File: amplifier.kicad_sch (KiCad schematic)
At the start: 14 parts, among them U1 OPA2188, U3 ADS1254E

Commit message: added simulation
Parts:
- added FB4: FerriteBead, Inductor_SMD:L_0402_1005Metric, symbol Device:FerriteBead
- added R61: 1500, symbol Device:R
- added V1: 3, symbol Simulation_SPICE:VDC
- added V12, V2: 2, symbol Simulation_SPICE:VDC
- added V4: VSIN, symbol Simulation_SPICE:VSIN
- C17: renamed from C1; value 1u -> 10u
- R23: renamed from R2; value 3k3 -> 3300
- R25: renamed from R4; value 2870 -> 20500
- R27: renamed from R6; value 5k9 -> 23700
- renumbered C5 to C18, C6 to C19, C2 to C20, C4 to C21, R3 to R24, R5 to R26, R7 to R28, R8 to R29, U3 to U9
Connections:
- net +2V048: now also V2.1
- net +2V93: now also V1.1
- net -2V048: now also R61.2, V12.2
- net Ain: now also FB4.2; no longer R23.2
- net GND renamed 0
- net 0: now also V1.2, V12.1, V2.2, V4.2
- new net: FB4.1, R23.2, R61.1, V4.1
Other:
- moved on the sheet: C17, C18, C19

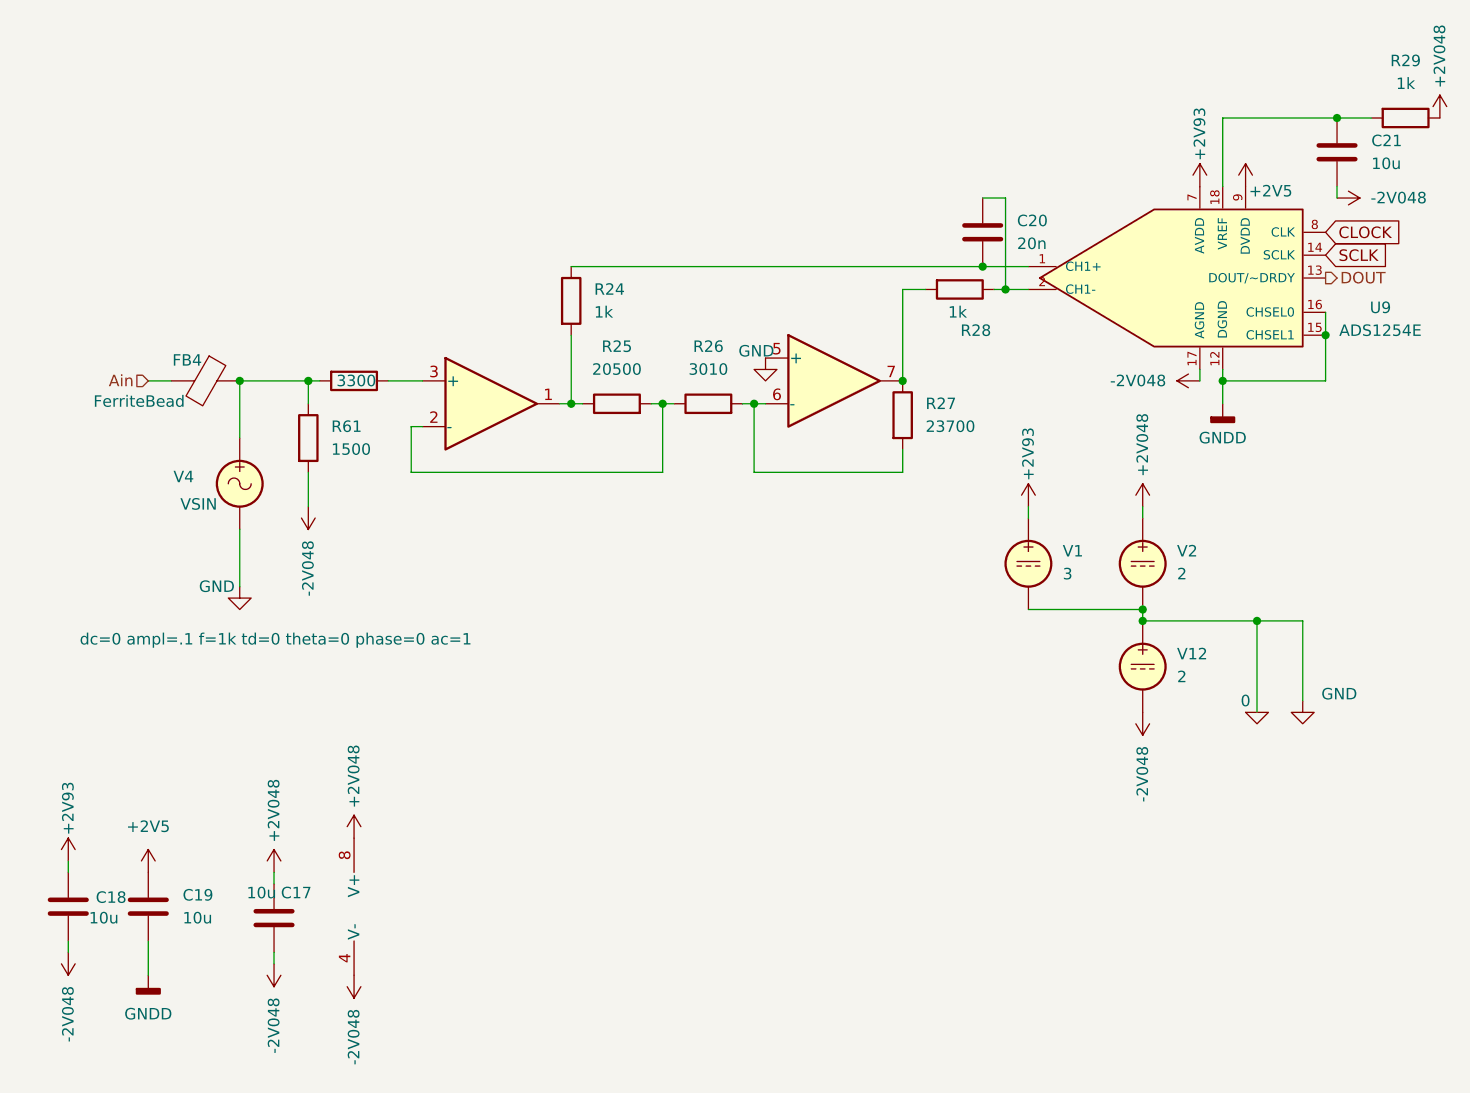
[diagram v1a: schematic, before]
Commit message: added components, updated pcb-routing
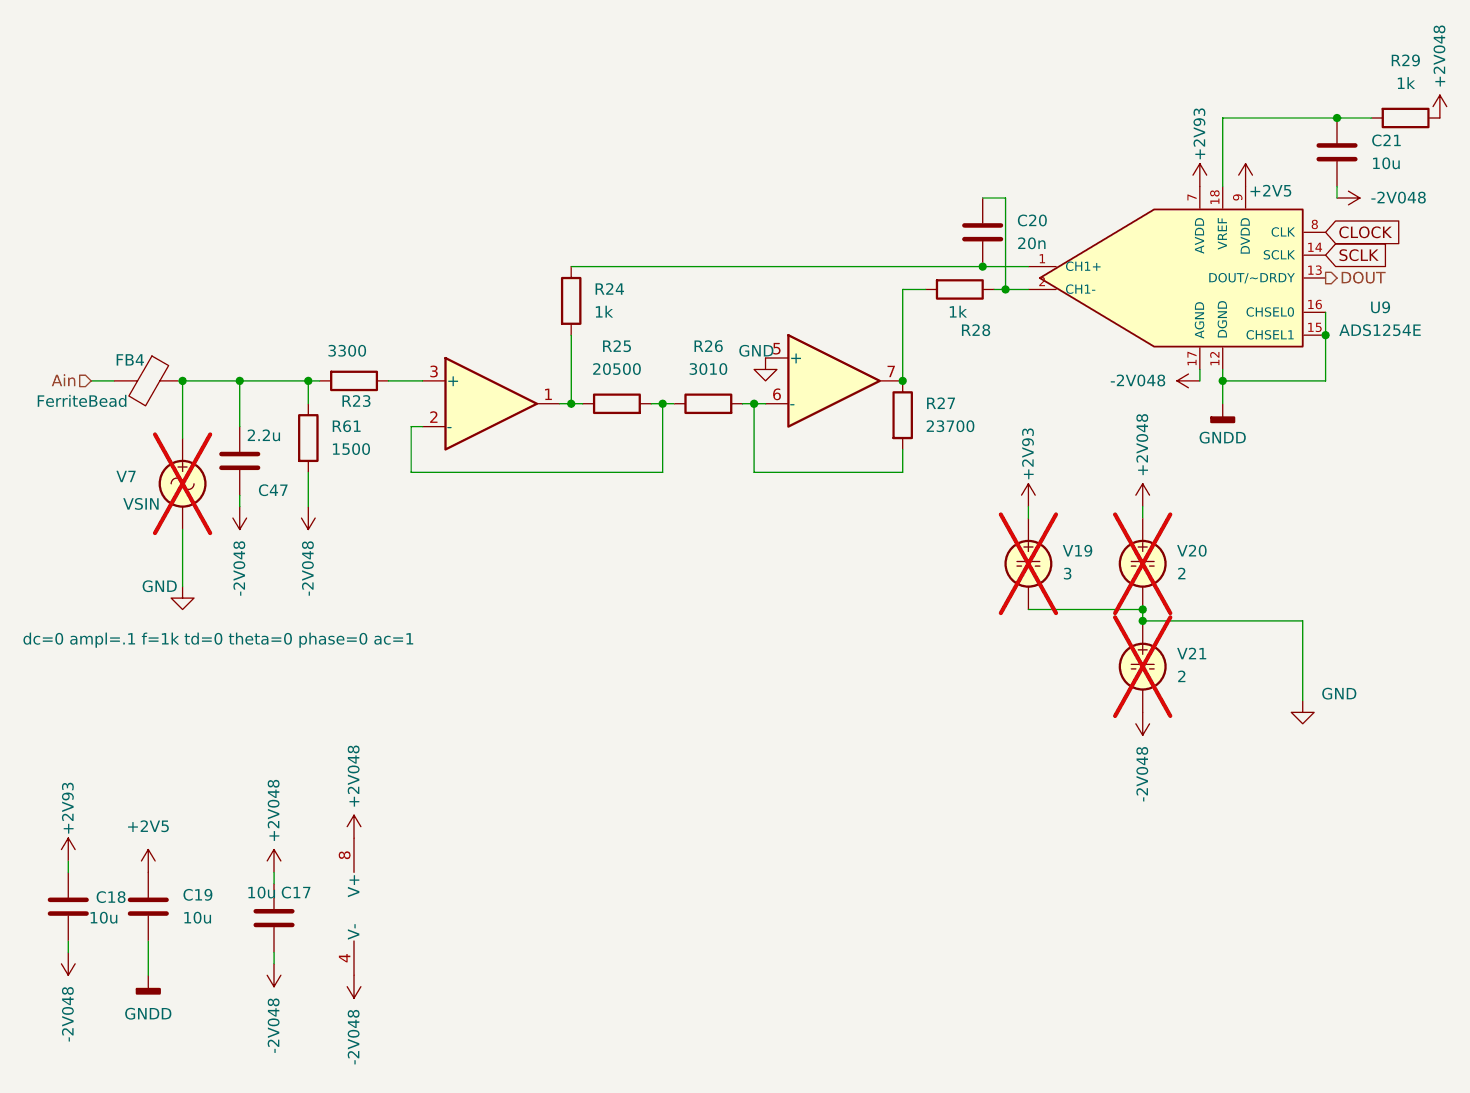
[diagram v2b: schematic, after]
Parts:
- added C47: 2.2u, Capacitor_SMD:C_0603_1608Metric, symbol Device:C
- C17, C18, C19, C21: footprint (none) -> Capacitor_SMD:C_0603_1608Metric; LCSC (none) -> C19702
- C20: footprint (none) -> Capacitor_SMD:C_0402_1005Metric; LCSC (none) -> C5448807
- FB4: LCSC (none) -> C76884
- R23: footprint (none) -> Resistor_SMD:R_0402_1005Metric; LCSC (none) -> C25890
- R24, R28, R29: footprint (none) -> Resistor_SMD:R_0402_1005Metric; LCSC (none) -> C11702
- R25: footprint (none) -> Resistor_SMD:R_0402_1005Metric; LCSC (none) -> C57105
- R26: footprint (none) -> Resistor_SMD:R_0402_1005Metric; LCSC (none) -> C25889
- R27: footprint (none) -> Resistor_SMD:R_0402_1005Metric; LCSC (none) -> C82134
- R61: footprint (none) -> Resistor_SMD:R_0402_1005Metric; LCSC (none) -> C25867
- U8: renamed from U1; value OPA2188 -> OPA2188AIDR; footprint (none) -> Package_SO:SOIC-8_3.9x4.9mm_P1.27mm; LCSC (none) -> C17271
- U9: footprint ADS1254E -> Package_SO:QSOP-20_3.9x8.7mm_P0.635mm; LCSC (none) -> C486047
- V19: renamed from V1; now not fitted
- V20: renamed from V2; now not fitted
- V21: renamed from V12; now not fitted
- V7: renamed from V4; now not fitted
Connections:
- net -2V048: now also C47.2
- net at FB4.1, R23.2, R61.1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: now also C47.1
- net 0 renamed GND
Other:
- moved on the sheet: FB4

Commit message: layout v2
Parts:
- C47: value 2.2u -> 100n; footprint Capacitor_SMD:C_0603_1608Metric -> Capacitor_SMD:C_0402_1005Metric; LCSC C1607 -> C880295
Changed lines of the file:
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@@
 			)
 		)
-		(property "Value" "2.2u"
+		(property "Value" "100n"
 			(at 42.672 60.706 0)
 			(effects
@@
 			)
 		)
-		(property "Footprint" "Capacitor_SMD:C_0603_1608Metric"
+		(property "Footprint" "Capacitor_SMD:C_0402_1005Metric"
 			(at 42.8752 67.31 0)
 			(effects
@@
 			)
 		)
-		(property "Description" "10V 2.2uF X5R ±10%"
+		(property "Description" "10V 100nF X7R ±10%"
 			(at 41.91 63.5 0)
 			(effects
@@
 			)
 		)
-		(property "LCSC" "C1607"
+		(property "LCSC" "C880295"
 			(at 41.91 63.5 0)
 			(effects
